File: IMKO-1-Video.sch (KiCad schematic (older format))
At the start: 13 parts, among them U18 82S129, U19 74LS244, U20 74LS244, U23 74LS86, U24 74LS163, U25 74LS00, U26 74LS374

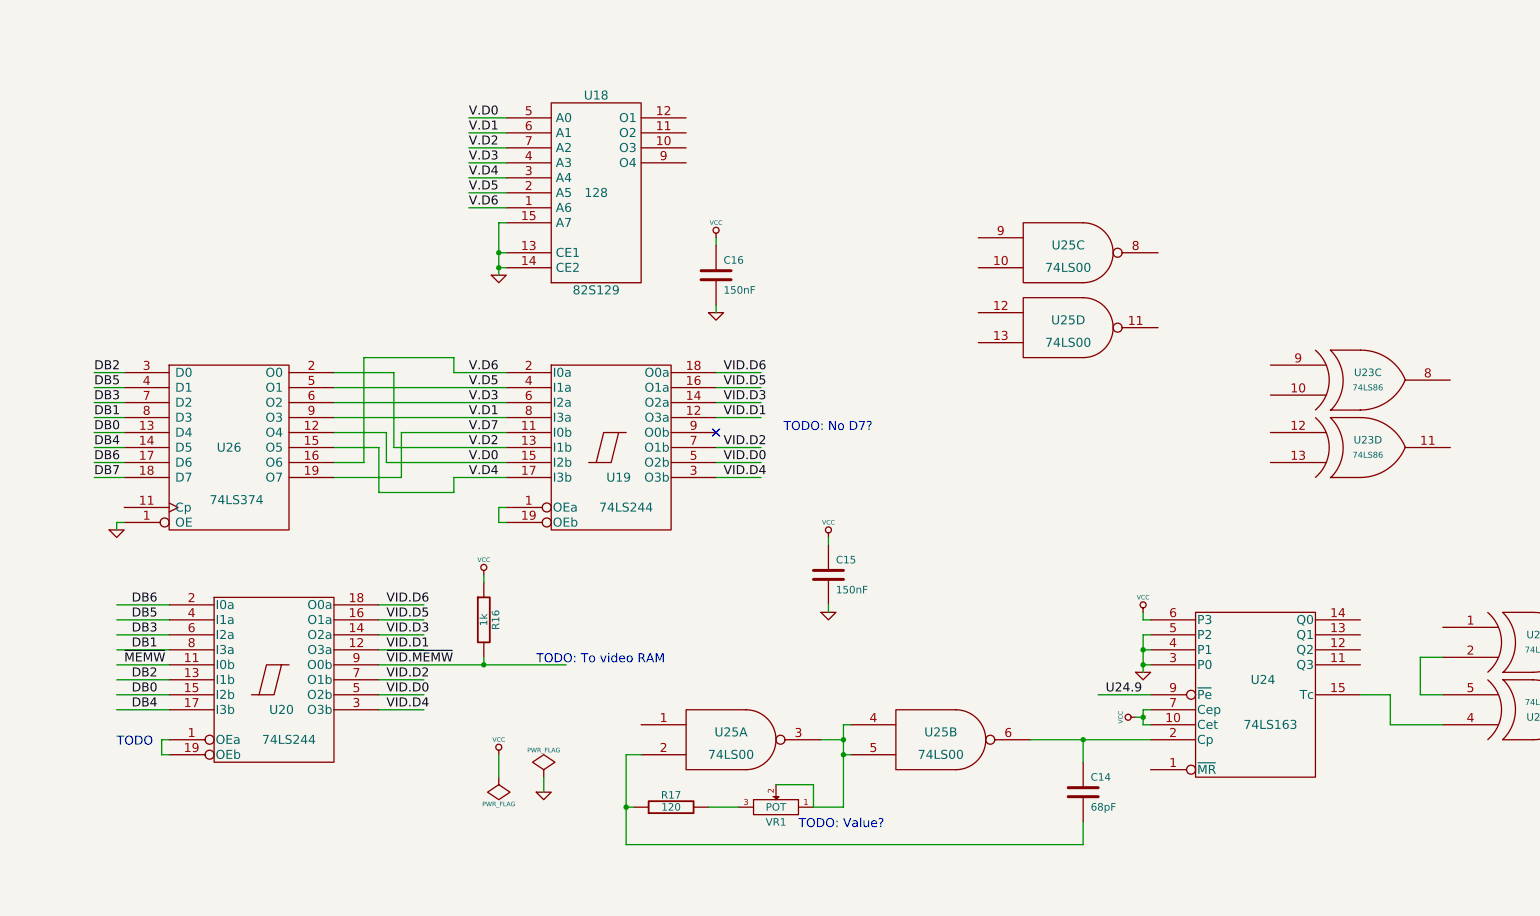
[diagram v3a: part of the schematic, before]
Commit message: Added U22
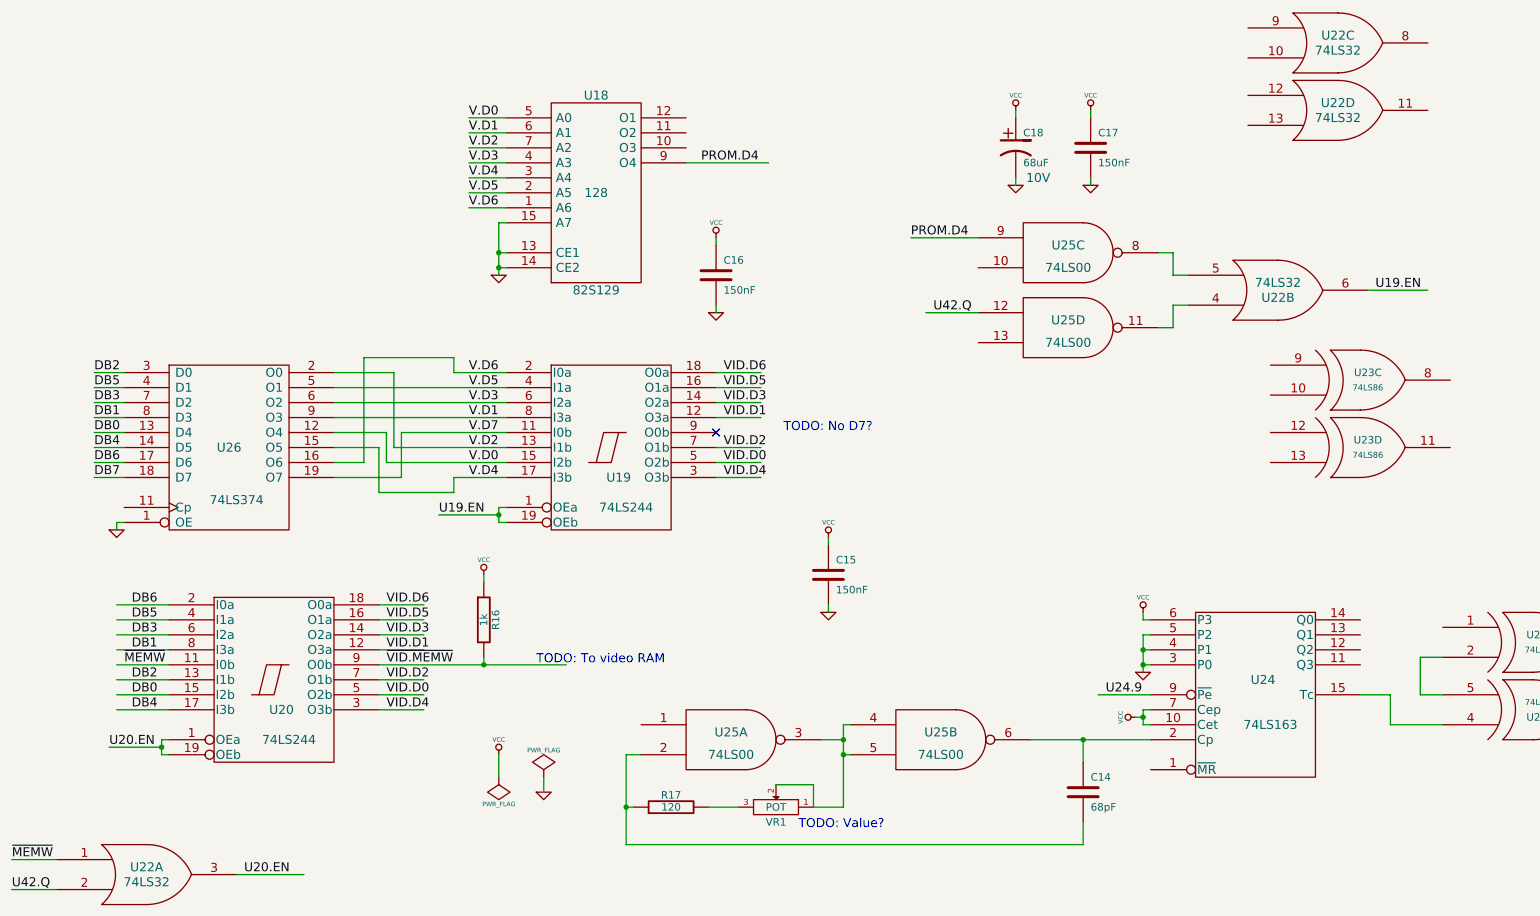
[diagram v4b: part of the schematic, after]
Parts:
- added C17: 150nF, symbol C
- added C18: 68uF, symbol CP1
- added U22: 74LS32, symbol 74LS32
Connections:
- net labels added: PROM.D4, U19.EN, U20.EN, U42.Q
- wire segments 113 -> 132
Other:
- note removed: "TODO"
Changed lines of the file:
@@
-EESchema Schematic File Version 2  date Wed 10 Oct 2012 09:46:06 PM EEST
+EESchema Schematic File Version 2  date Wed 10 Oct 2012 11:21:39 PM EEST
 LIBS:power
 LIBS:device
@@
 Text Notes 4250 7200 0    60   ~ 0
 TODO: To video RAM
-Text Notes 1450 7750 0    60   ~ 0
-TODO
 Wire Wire Line
 	2900 5950 3350 5950
@@
 Text Notes 11450 7600 0    60   ~ 0
 TODO: Name
+$Comp
+L 74LS32 U22
+U 1 1 5075CD80
+P 1650 8600
+F 0 "U22" H 1650 8650 60  0000 C CNN
+F 1 "74LS32" H 1650 8550 60  0000 C CNN
+	1    1650 8600
+	1    0    0    -1
+$EndComp
+$Comp
+L 74LS32 U22
+U 2 1 5075CD8D
+P 9200 4700
+F 0 "U22" H 9200 4750 60  0000 C CNN
+F 1 "74LS32" H 9200 4650 60  0000 C CNN
+	2    9200 4700
+	1    0    0    1
+$EndComp
+$Comp
+L 74LS32 U22
+U 3 1 5075CDB4
+P 9600 3050
+F 0 "U22" H 9600 3100 60  0000 C CNN
+F 1 "74LS32" H 9600 3000 60  0000 C CNN
+	3    9600 3050
+	1    0    0    -1
+$EndComp
+$Comp
+L 74LS32 U22
+U 4 1 5075CDCD
+P 9600 3500
+F 0 "U22" H 9600 3550 60  0000 C CNN
+F 1 "74LS32" H 9600 3450 60  0000 C CNN
+	4    9600 3500
+	1    0    0    -1
+$EndComp
+Text Label 750  8500 0    60   ~ 0
+~MEMW
+Wire Wire Line
+	1050 8500 750  8500
+Wire Wire Line
+	7200 4850 6850 4850
+Text Label 6900 4850 0    60   ~ 0
+U42.Q
+Text Label 750  8700 0    60   ~ 0
+U42.Q
+Wire Wire Line
+	1400 7750 1750 7750
+Connection ~ 1750 7750
+Wire Wire Line
+	1050 8700 750  8700
+Text Label 1400 7750 0    60   ~ 0
+U20.EN
+Wire Wire Line
+	8400 4450 8500 4450
+Wire Wire Line
+	8500 4450 8500 4600
+Wire Wire Line
+	8500 4600 8600 4600
+Wire Wire Line
+	8600 4800 8500 4800
+Wire Wire Line
+	8500 4800 8500 4950
+Wire Wire Line
+	8500 4950 8400 4950
+Wire Wire Line
+	9800 4700 10200 4700
+Text Label 9850 4700 0    60   ~ 0
+U19.EN
+Text Label 3600 6200 0    60   ~ 0
+U19.EN
+Wire Wire Line
+	3600 6200 4000 6200
+Connection ~ 4000 6200
+Wire Wire Line
+	2250 8600 2700 8600
+Text Label 2300 8600 0    60   ~ 0
+U20.EN
+$Comp
+L C C17
+U 1 1 5075D6B0
+P 7950 3750
+F 0 "C17" H 8000 3850 50  0000 L CNN
+F 1 "150nF" H 8000 3650 50  0000 L CNN
+	1    7950 3750
+	1    0    0    -1
+$EndComp
+$Comp
+L GND #PWR015
+U 1 1 5075D6B6
+P 7950 4000
+F 0 "#PWR015" H 7950 4000 30  0001 C CNN
+F 1 "GND" H 7950 3930 30  0001 C CNN
+	1    7950 4000
+	1    0    0    -1
+$EndComp
+$Comp
+L VCC #PWR016
+U 1 1 5075D6BC
+P 7950 3500
+F 0 "#PWR016" H 7950 3600 30  0001 C CNN
+F 1 "VCC" H 7950 3600 30  0000 C CNN
+	1    7950 3500
+	1    0    0    -1
+$EndComp
+Wire Wire Line
+	7950 3500 7950 3550
+Wire Wire Line
+	7950 3950 7950 4000
+Wire Wire Line
+	5250 3850 5800 3850
+Text Label 5350 3850 0    60   ~ 0
+PROM.D4
+Text Label 6750 4350 0    60   ~ 0
+PROM.D4
+Wire Wire Line
+	7200 4350 6750 4350
+$Comp
+L CP1 C18
+U 1 1 5075DBCD
+P 7450 3750
+F 0 "C18" H 7500 3850 50  0000 L CNN
+F 1 "68uF" H 7500 3650 50  0000 L CNN
+F 4 "10V" H 7600 3550 60  0000 C CNN "Field4"
+	1    7450 3750
+	1    0    0    -1
+$EndComp
+$Comp
+L VCC #PWR?
+U 1 1 5075DBDA
+P 7450 3500
+F 0 "#PWR?" H 7450 3600 30  0001 C CNN
+F 1 "VCC" H 7450 3600 30  0000 C CNN
+	1    7450 3500
+	1    0    0    -1
+$EndComp
+$Comp
+L GND #PWR?
+U 1 1 5075DBE0
+P 7450 4000
+F 0 "#PWR?" H 7450 4000 30  0001 C CNN
+F 1 "GND" H 7450 3930 30  0001 C CNN
+	1    7450 4000
+	1    0    0    -1
+$EndComp
+Wire Wire Line
+	7450 3550 7450 3500
+Wire Wire Line
+	7450 3950 7450 4000
 $EndSCHEMATC

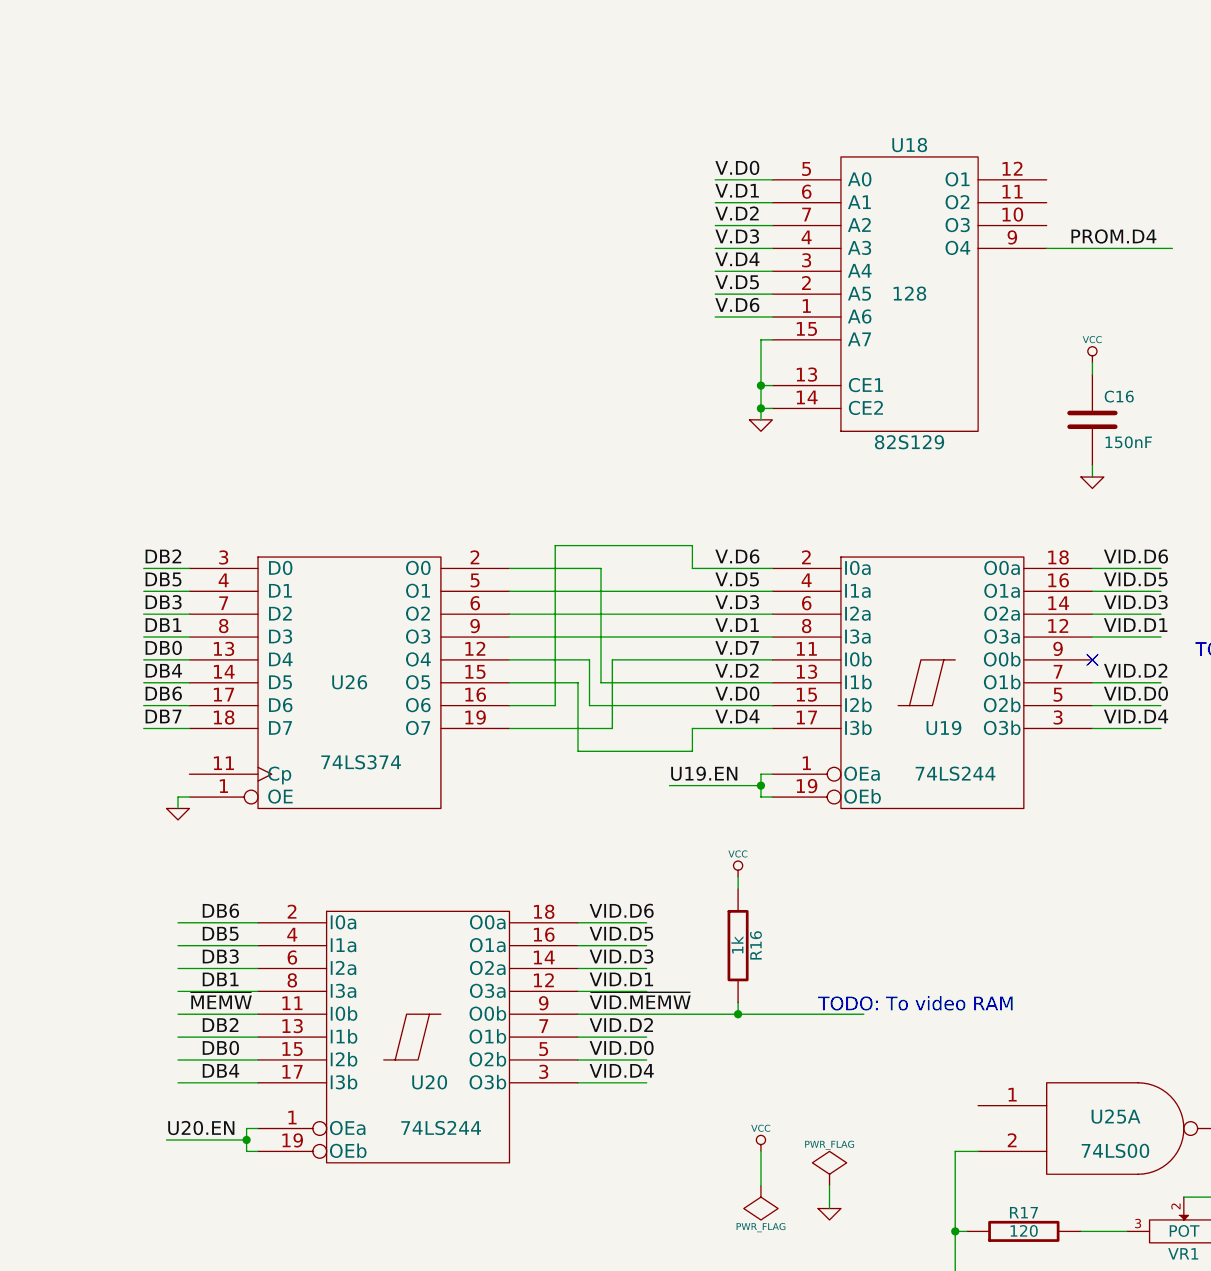
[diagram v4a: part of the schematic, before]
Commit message: Added Rs
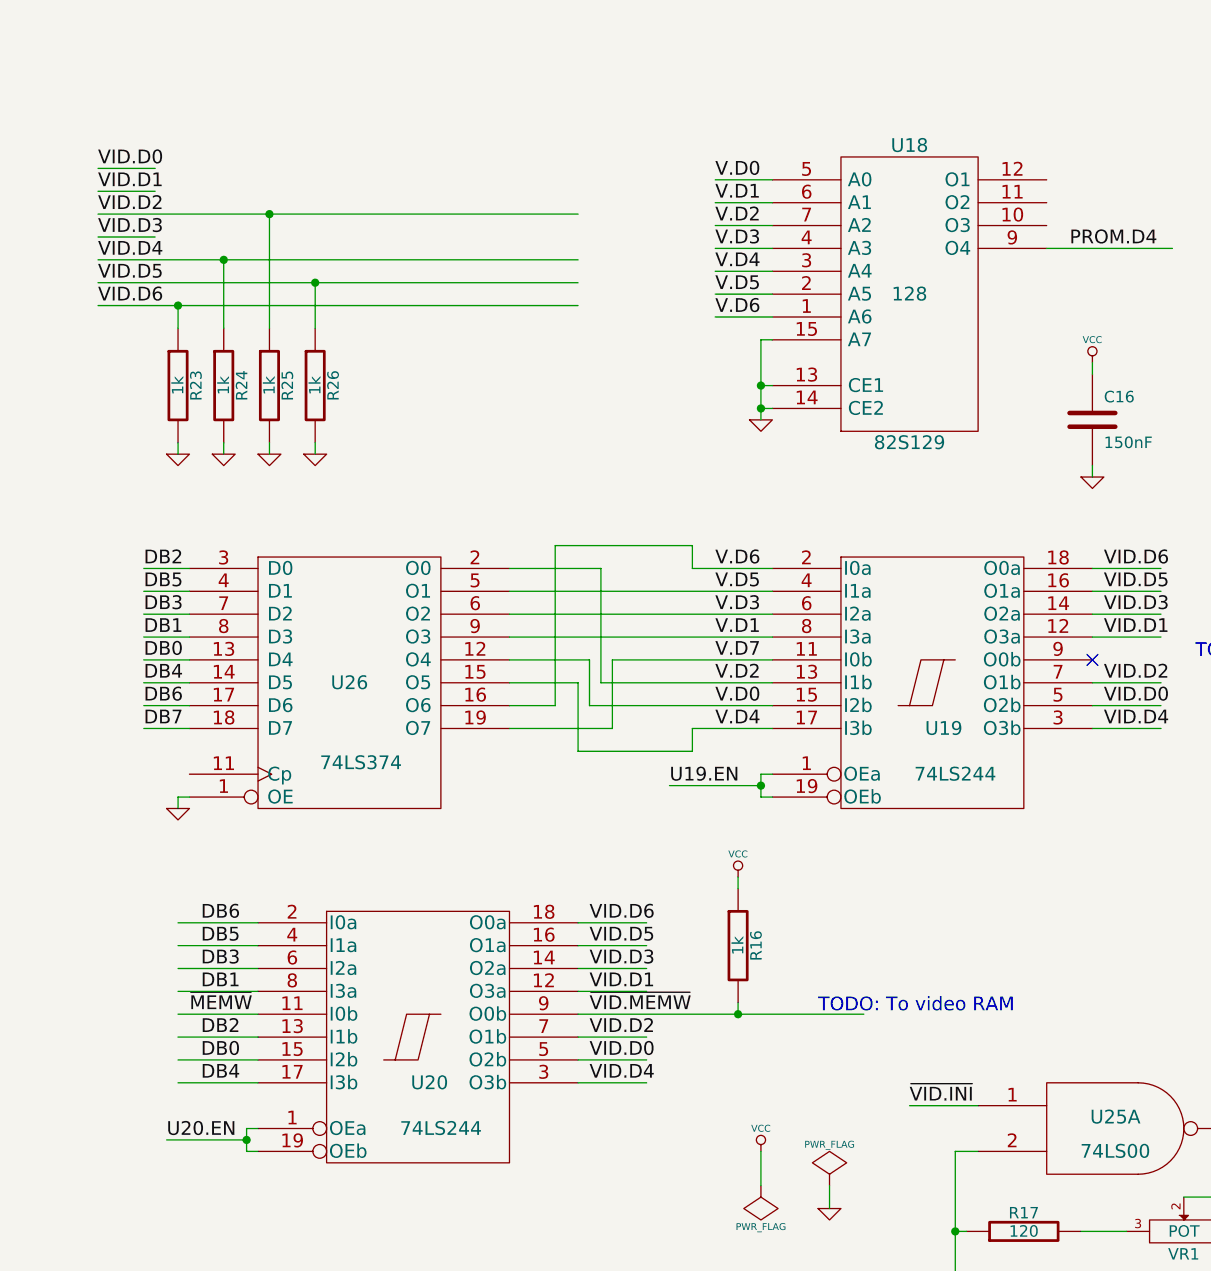
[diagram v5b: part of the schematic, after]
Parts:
- added R23, R24, R25, R26: 1k, symbol R
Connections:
- net labels added: ~VID.INI
- wire segments 132 -> 148
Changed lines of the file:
@@
-EESchema Schematic File Version 2  date Wed 10 Oct 2012 11:21:39 PM EEST
+EESchema Schematic File Version 2  date Wed 10 Oct 2012 11:46:42 PM EEST
 LIBS:power
 LIBS:device
@@
 $EndComp
 $Comp
-L VCC #PWR?
+L VCC #PWR017
 U 1 1 5075DBDA
 P 7450 3500
-F 0 "#PWR?" H 7450 3600 30  0001 C CNN
+F 0 "#PWR017" H 7450 3600 30  0001 C CNN
 F 1 "VCC" H 7450 3600 30  0000 C CNN
 	1    7450 3500
@@
 $EndComp
 $Comp
-L GND #PWR?
+L GND #PWR018
 U 1 1 5075DBE0
 P 7450 4000
-F 0 "#PWR?" H 7450 4000 30  0001 C CNN
+F 0 "#PWR018" H 7450 4000 30  0001 C CNN
 F 1 "GND" H 7450 3930 30  0001 C CNN
 	1    7450 4000
@@
 Wire Wire Line
 	7450 3950 7450 4000
+Wire Wire Line
+	1350 3500 1100 3500
+Wire Wire Line
+	1350 3600 1100 3600
+Wire Wire Line
+	1100 3700 3200 3700
+Wire Wire Line
+	1350 3800 1100 3800
+Wire Wire Line
+	1100 3900 3200 3900
+Wire Wire Line
+	1100 4000 3200 4000
+Wire Wire Line
+	1100 4100 3200 4100
+Text Label 1100 3700 0    60   ~ 0
+VID.D2
+Text Label 1100 3500 0    60   ~ 0
+VID.D0
+Text Label 1100 3900 0    60   ~ 0
+VID.D4
+Text Label 1100 3600 0    60   ~ 0
+VID.D1
+Text Label 1100 3800 0    60   ~ 0
+VID.D3
+Text Label 1100 4000 0    60   ~ 0
+VID.D5
+Text Label 1100 4100 0    60   ~ 0
+VID.D6
+$Comp
+L R R23
+U 1 1 5075DEC0
+P 1450 4450
+F 0 "R23" V 1530 4450 50  0000 C CNN
+F 1 "1k" V 1450 4450 50  0000 C CNN
+	1    1450 4450
+	1    0    0    -1
+$EndComp
+Wire Wire Line
+	1450 4100 1450 4200
+Connection ~ 1450 4100
+$Comp
+L GND #PWR019
+U 1 1 5075E00A
+P 1450 4750
+F 0 "#PWR019" H 1450 4750 30  0001 C CNN
+F 1 "GND" H 1450 4680 30  0001 C CNN
+	1    1450 4750
+	1    0    0    -1
+$EndComp
+Wire Wire Line
+	1450 4750 1450 4700
+$Comp
+L R R24
+U 1 1 5075E0AA
+P 1650 4450
+F 0 "R24" V 1730 4450 50  0000 C CNN
+F 1 "1k" V 1650 4450 50  0000 C CNN
+	1    1650 4450
+	1    0    0    -1
+$EndComp
+$Comp
+L GND #PWR020
+U 1 1 5075E0B1
+P 1650 4750
+F 0 "#PWR020" H 1650 4750 30  0001 C CNN
+F 1 "GND" H 1650 4680 30  0001 C CNN
+	1    1650 4750
+	1    0    0    -1
+$EndComp
+Wire Wire Line
+	1650 4750 1650 4700
+Wire Wire Line
+	1650 3900 1650 4200
+Connection ~ 1650 3900
+$Comp
+L R R25
+U 1 1 5075E1FD
+P 1850 4450
+F 0 "R25" V 1930 4450 50  0000 C CNN
+F 1 "1k" V 1850 4450 50  0000 C CNN
+	1    1850 4450
+	1    0    0    -1
+$EndComp
+$Comp
+L GND #PWR021
+U 1 1 5075E203
+P 1850 4750
+F 0 "#PWR021" H 1850 4750 30  0001 C CNN
+F 1 "GND" H 1850 4680 30  0001 C CNN
+	1    1850 4750
+	1    0    0    -1
+$EndComp
+Wire Wire Line
+	1850 4750 1850 4700
+$Comp
+L R R26
+U 1 1 5075E2B7
+P 2050 4450
+F 0 "R26" V 2130 4450 50  0000 C CNN
+F 1 "1k" V 2050 4450 50  0000 C CNN
+	1    2050 4450
+	1    0    0    -1
+$EndComp
+$Comp
+L GND #PWR022
+U 1 1 5075E2BD
+P 2050 4750
+F 0 "#PWR022" H 2050 4750 30  0001 C CNN
+F 1 "GND" H 2050 4680 30  0001 C CNN
+	1    2050 4750
+	1    0    0    -1
+$EndComp
+Wire Wire Line
+	2050 4750 2050 4700
+Wire Wire Line
+	1850 4200 1850 3700
+Connection ~ 1850 3700
+Wire Wire Line
+	2050 4000 2050 4200
+Connection ~ 2050 4000
+Wire Wire Line
+	4650 7600 4950 7600
+Text Label 4650 7600 0    60   ~ 0
+~VID.INI
 $EndSCHEMATC
